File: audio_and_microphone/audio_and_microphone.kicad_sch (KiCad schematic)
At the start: 36 parts, among them J2 Conn_01x02, U1 LM4810, U2 ${SIM.PARAMS}, U3 ${SIM.PARAMS}

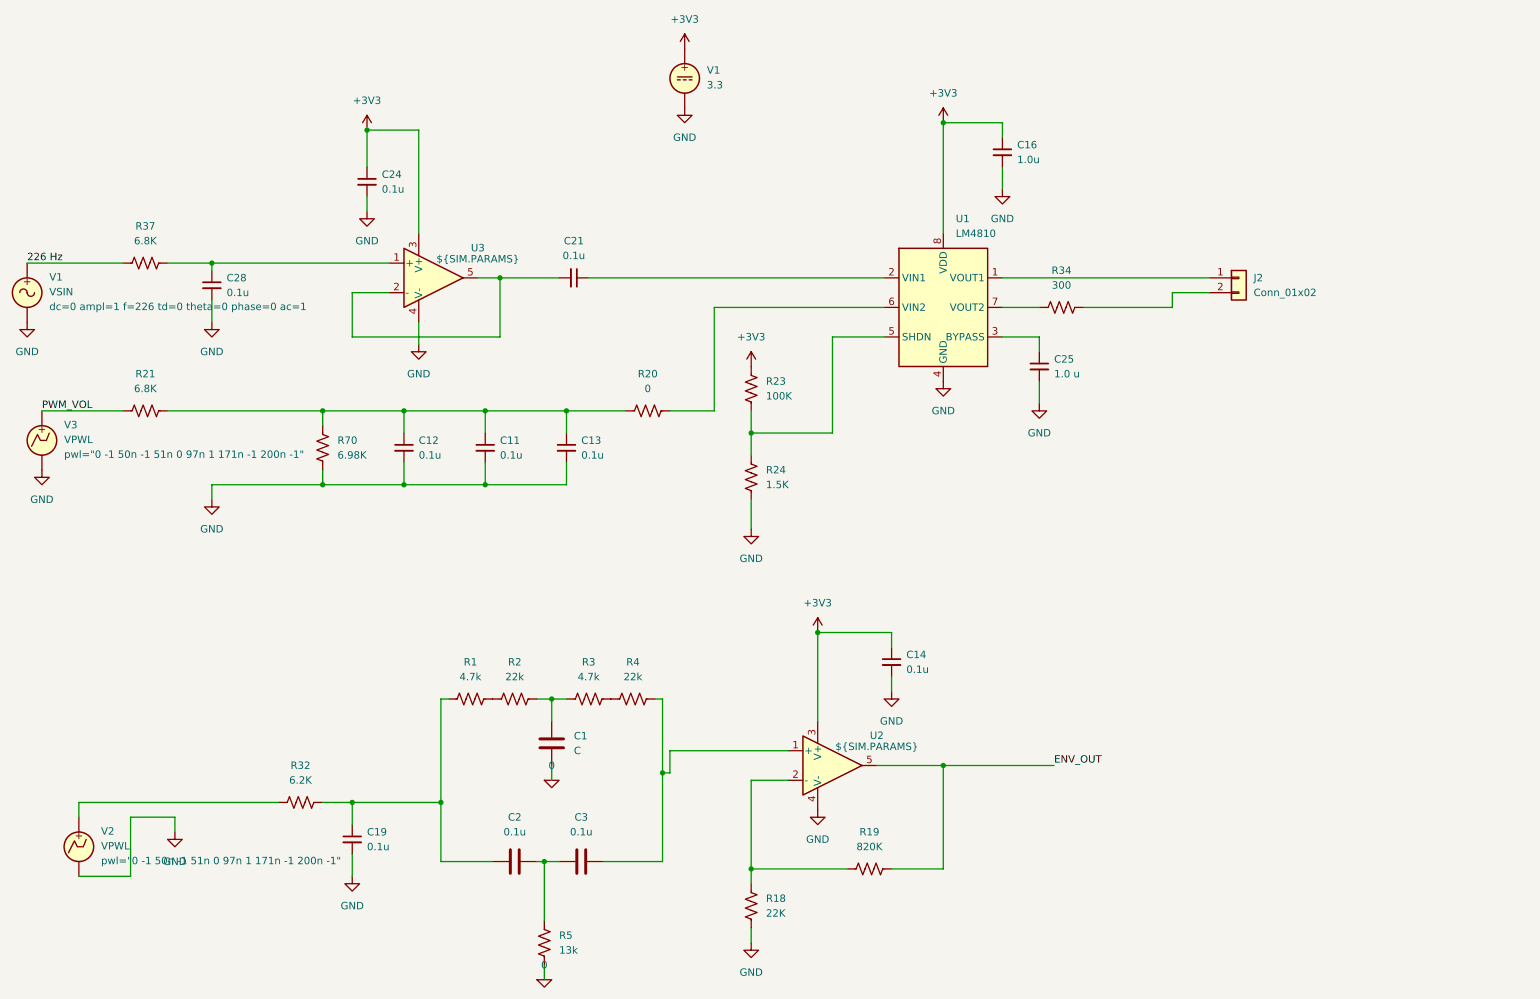
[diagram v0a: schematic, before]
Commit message: deleted audio circuit from microhpone
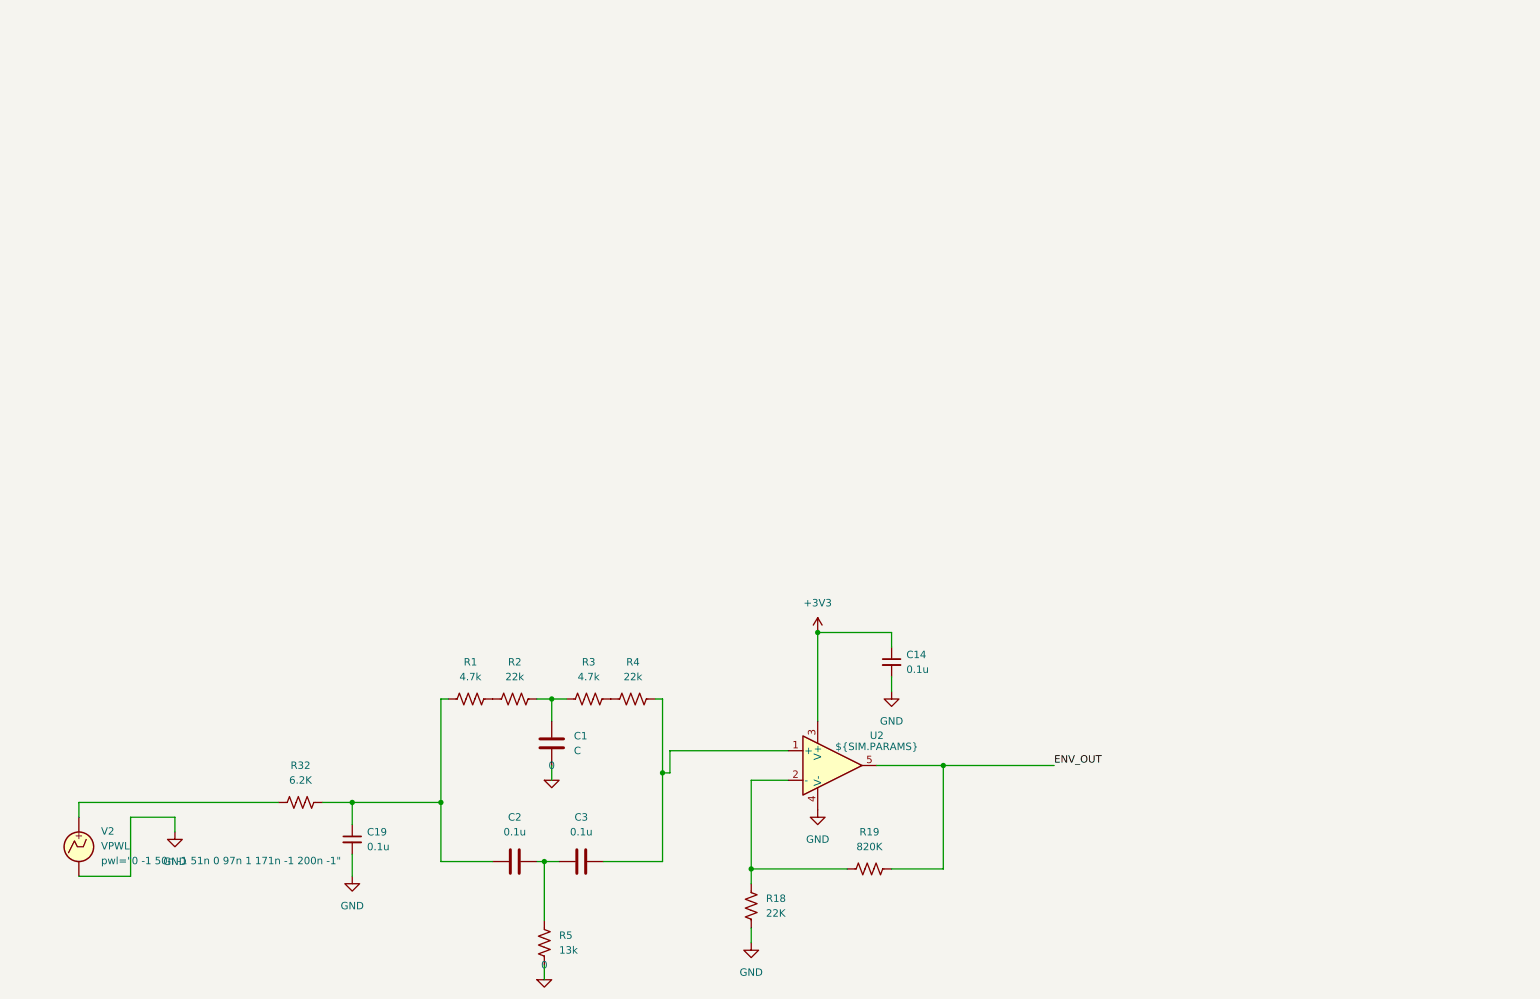
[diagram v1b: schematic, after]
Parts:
- removed C11, C12, C13, C21, C24, C28: 0.1u, symbol Device:C_Small
- removed C16: 1.0u, symbol Device:C_Small
- removed C25: 1.0 u, symbol Device:C_Small
- removed J2: Conn_01x02, symbol Connector_Generic:Conn_01x02
- removed R20: 0, symbol Device:R_US
- removed R21, R37: 6.8K, symbol Device:R_US
- removed R23: 100K, symbol Device:R_US
- removed R24: 1.5K, symbol Device:R_US
- removed R34: 300, symbol Device:R_US
- removed R70: 6.98K, symbol Device:R_US
- removed U1: LM4810, Package_SO:TSSOP-8_3x3mm_P0.65mm, symbol Amplifier_Audio:LM4810
- removed U3: ${SIM.PARAMS}, symbol Simulation_SPICE:OPAMP
- removed V1: VSIN, symbol Simulation_SPICE:VSIN
- removed V1: 3.3, symbol Simulation_SPICE:VDC
- removed V3: VPWL, symbol Simulation_SPICE:VPWL

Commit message: created inital pcb layout
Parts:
- C1, C14, C19, C2, C3: footprint (none) -> Capacitor_SMD:C_0201_0603Metric
- R1, R18, R19, R2, R3, R32, R4, R5: footprint (none) -> Resistor_SMD:R_0201_0603Metric
- U6: renamed from U2; footprint (none) -> Package_TO_SOT_SMD:SOT-23-5
- V2: footprint (none) -> Connector_PinHeader_2.54mm:PinHeader_1x02_P2.54mm_Vertical
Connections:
- net 0 is gone; now on net GND: C1.2, R5.2
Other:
- moved on the sheet: C1, C14, C19, C2, C3, R1, R18, R19, R2, R3, R32, R4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

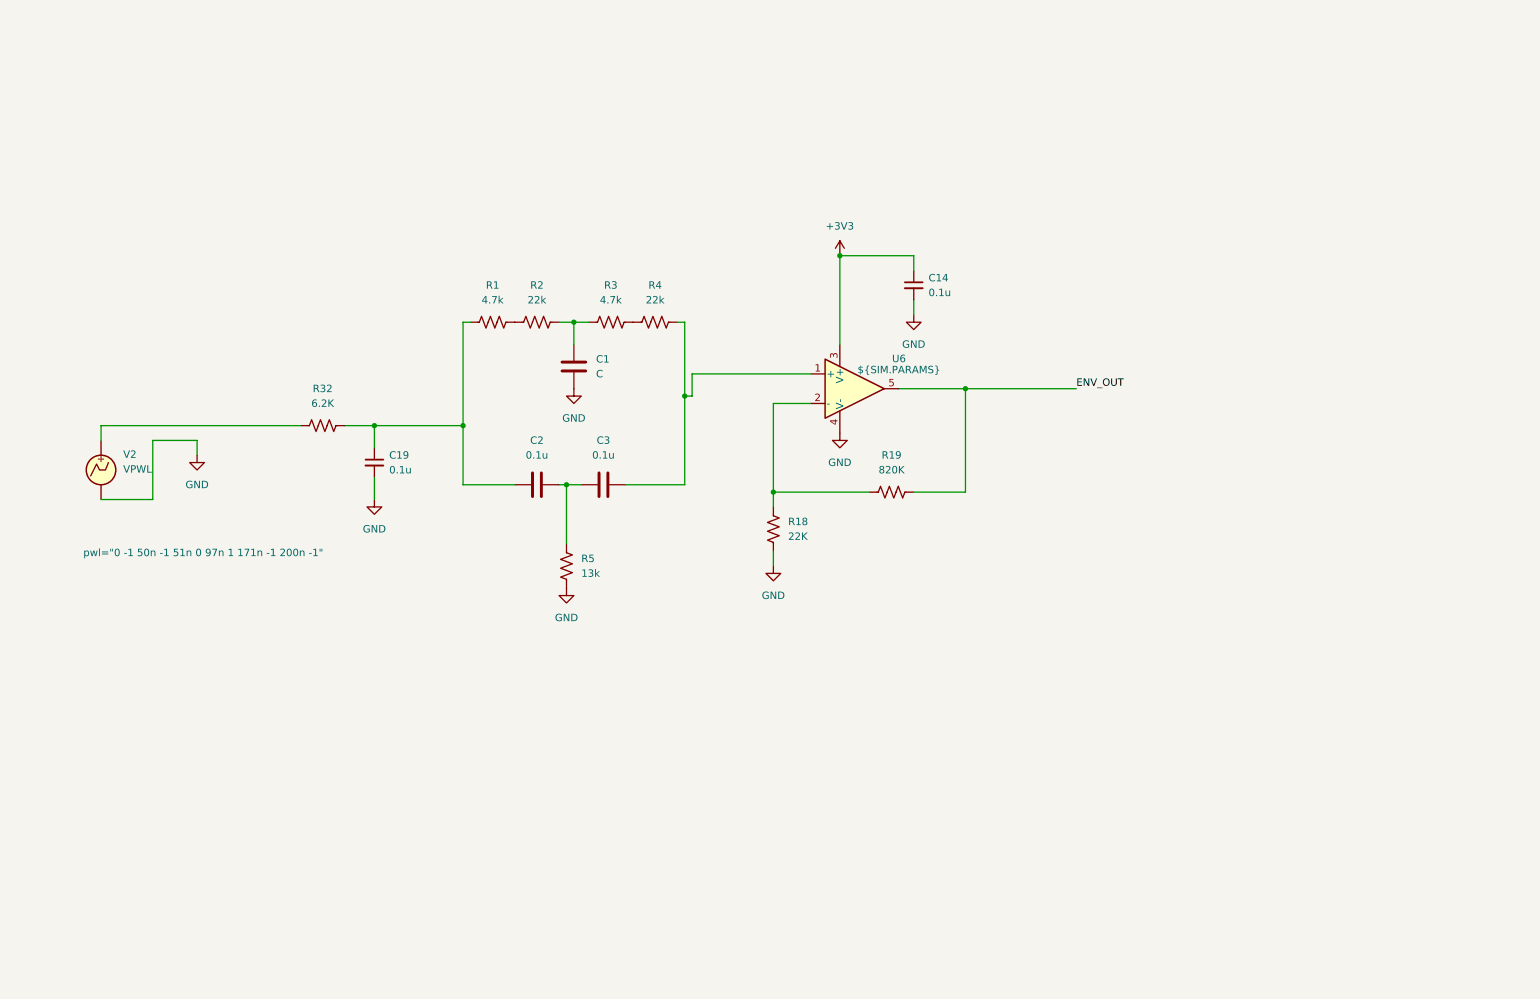
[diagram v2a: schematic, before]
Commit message: updated pcb with components and locked pin holders NON THRU
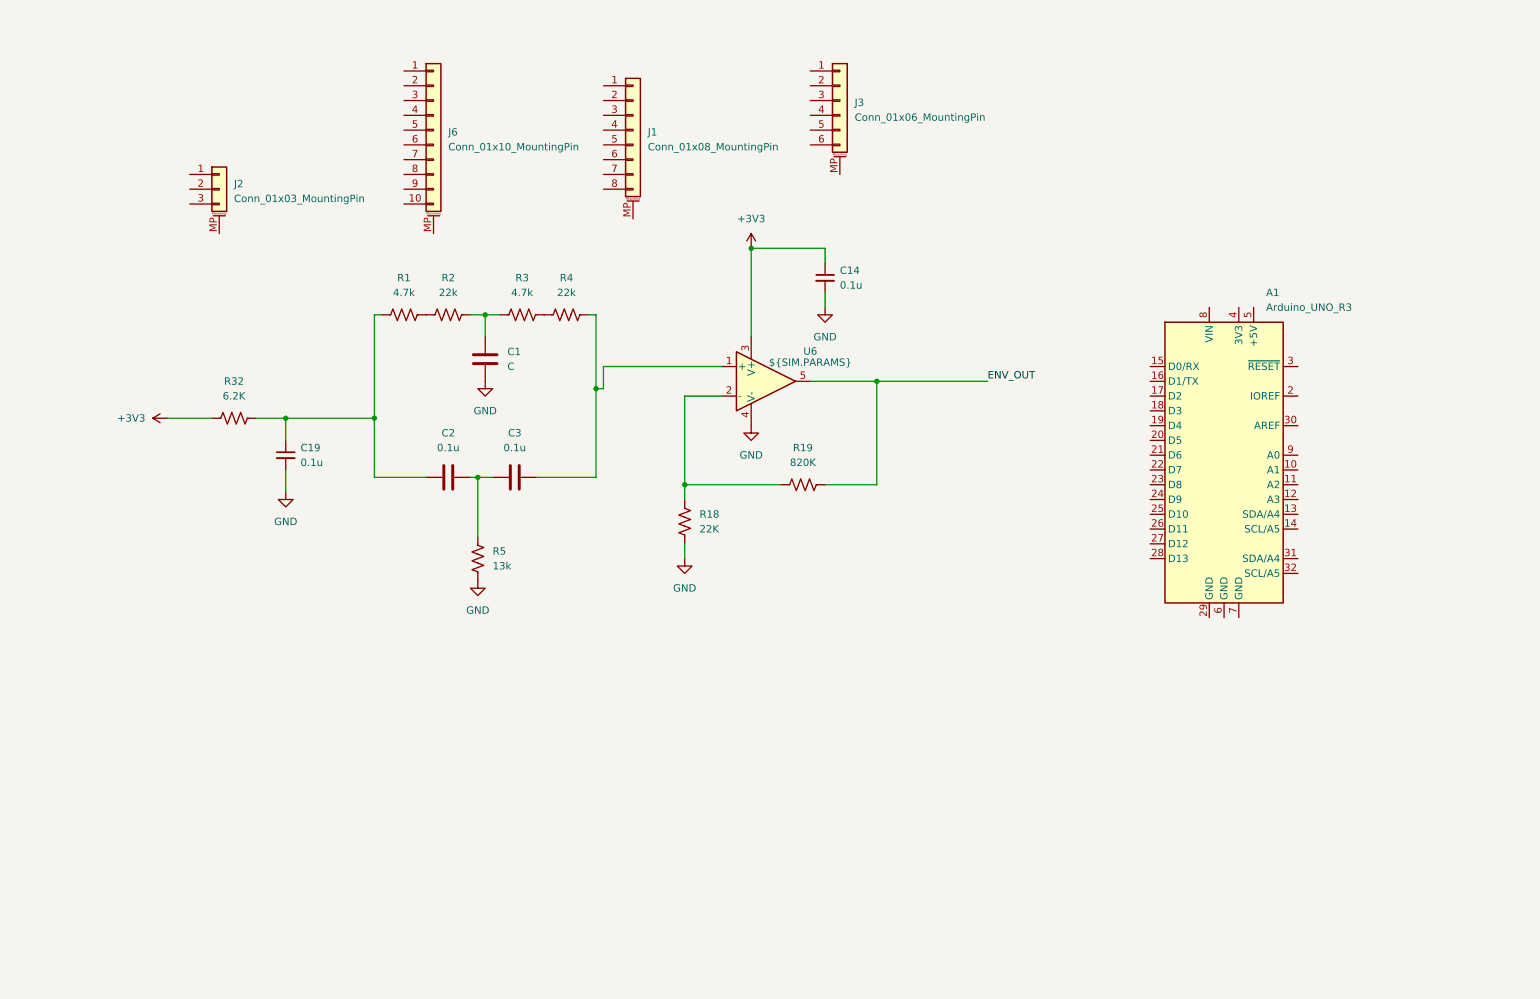
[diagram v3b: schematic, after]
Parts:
- removed V2: VPWL, Connector_PinHeader_2.54mm:PinHeader_1x02_P2.54mm_Vertical, symbol Simulation_SPICE:VPWL
- added A1: Arduino_UNO_R3, Module:Arduino_UNO_R3, symbol MCU_Module:Arduino_UNO_R3
- added J1: Conn_01x08_MountingPin, Connector_PinHeader_2.54mm:PinHeader_1x08_P2.54mm_Vertical, symbol Connector_Generic_MountingPin:Conn_01x08_MountingPin
- added J2: Conn_01x03_MountingPin, Connector_Harwin:Harwin_M20-89003xx_1x03_P2.54mm_Horizontal, symbol Connector_Generic_MountingPin:Conn_01x03_MountingPin
- added J3: Conn_01x06_MountingPin, Connector_PinHeader_2.54mm:PinHeader_1x06_P2.54mm_Vertical, symbol Connector_Generic_MountingPin:Conn_01x06_MountingPin
- added J6: Conn_01x10_MountingPin, Connector_PinHeader_2.54mm:PinHeader_1x10_P2.54mm_Vertical, symbol Connector_Generic_MountingPin:Conn_01x10_MountingPin
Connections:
- net +3V3: now also R32.2
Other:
- moved on the sheet: C1, C14, C19, C2, C3, R1, R18, R19, R2, R3, R32, R4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

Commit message: updated pcb board with switch mechanisms for old vs new filters and tht pin holes
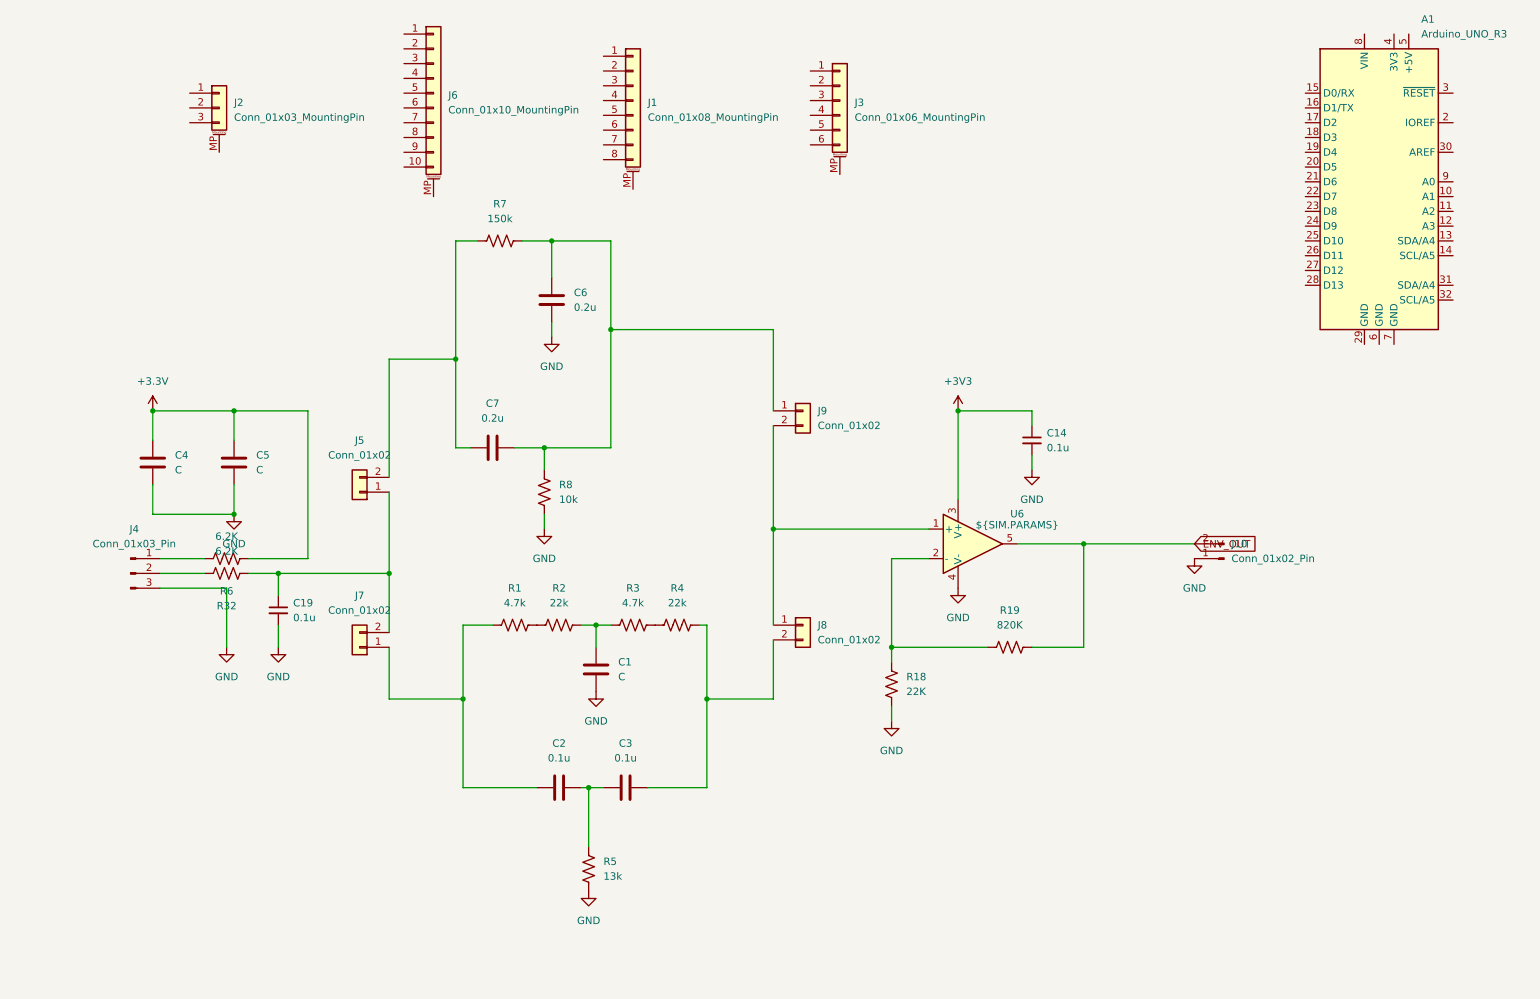
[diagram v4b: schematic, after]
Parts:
- added C4, C5: C, Capacitor_SMD:C_0603_1608Metric_Pad1.08x0.95mm_HandSolder, symbol Device:C
- added C6, C7: 0.2u, Capacitor_SMD:C_0603_1608Metric_Pad1.08x0.95mm_HandSolder, symbol Device:C
- added J10: Conn_01x02_Pin, Connector_PinHeader_2.54mm:PinHeader_1x02_P2.54mm_Vertical, symbol Connector:Conn_01x02_Pin
- added J4: Conn_01x03_Pin, Connector_PinHeader_2.54mm:PinHeader_1x03_P2.54mm_Vertical, symbol Connector:Conn_01x03_Pin
- added J5, J7, J8, J9: Conn_01x02, Connector_PinHeader_2.54mm:PinHeader_1x02_P2.54mm_Vertical, symbol Connector_Generic:Conn_01x02
- added R6: 6.2K, Resistor_SMD:R_0603_1608Metric_Pad0.98x0.95mm_HandSolder, symbol Device:R_US
- added R7: 150k, Resistor_SMD:R_0603_1608Metric_Pad0.98x0.95mm_HandSolder, symbol Device:R_US
- added R8: 10k, Resistor_SMD:R_0603_1608Metric_Pad0.98x0.95mm_HandSolder, symbol Device:R_US
- C1, C14, C19, C2, C3: footprint Capacitor_SMD:C_0201_0603Metric -> Capacitor_SMD:C_0603_1608Metric_Pad1.08x0.95mm_HandSolder
- R1, R18, R19, R2, R3, R32, R4, R5: footprint Resistor_SMD:R_0201_0603Metric -> Resistor_SMD:R_0603_1608Metric_Pad0.98x0.95mm_HandSolder
- U6: footprint Package_TO_SOT_SMD:SOT-23-5 -> Package_TO_SOT_SMD:TSOT-23-5_HandSoldering
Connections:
- net +3V3: no longer R32.2
- net ENV_OUT: now also J10.2 (Pin_2)
- net GND: now also C4.2, C5.2, C6.2, J10.1 (Pin_1), J4.3 (Pin_3), R8.2
- net at C2.1, R1.1: now also J7.1 (Pin_1); no longer C19.1, R32.1
- net at C3.2, R4.2: now also J8.2 (Pin_2); no longer U6.1 (+)
- new net: C7.1, J5.2 (Pin_2), R7.1
- new net: C6.1, C7.2, J9.1 (Pin_1), R7.2, R8.1
- new net: J4.1 (Pin_1), R6.2
- new net: J8.1 (Pin_1), J9.2 (Pin_2), U6.1 (+)
- new net: C19.1, J5.1 (Pin_1), J7.2 (Pin_2), R32.1
- new net: J4.2 (Pin_2), R32.2
- new net +3.3V: C4.1, C5.1, R6.1
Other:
- moved on the sheet: A1, C1, C14, C19, C2, C3, J1, J2, J6, R1, R18, R19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
